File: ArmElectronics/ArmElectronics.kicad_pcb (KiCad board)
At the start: 2 copper layers, 101 x 139 mm, 97 parts, among them J1 Raspberry_Pi_2_3, J10 AH1815 Breakout, J11 AH1815 Breakout, J12 AH1815 Breakout, J13 AH1815 Breakout, J14 AH1815 Breakout, J15 AH1815 Breakout, J16 AH1815 Breakout, J17 AH1815 Breakout, J18 AH1815 Breakout, J19 AH1815 Breakout, J2 Conn_01x14, J20 AH1815 Breakout, J21 1792245, J22 PA-09, J23 PA-09, J24 PA-09, J25 Solenoid, J26 Stepper Alternate Connection, J27 Computer Fan, J28 Computer Fan, J3 Encoder Breakout, J4 RasPi Power Out, J5 12V In, J6 Batt In, J7 Batt Out, J8 BNO055 QWIIC Conn, J9 AH1815 Breakout, Q1 Q_NMOS_GDSD, SW1 E-Stop, U1 Teensy4.1, U12 74LVC1G97, U13 74LVC1G97, U14 74LVC1G97, U15 74LVC1G97, U16 74LVC1G97, U17 74LVC1G97, U2 Pololu_2857, U3 MAX11601, U4 Pololu_2851, U5 Pololu_3730, U6 TB9051FTG, U7 TB9051FTG, U8 TB9051FTG

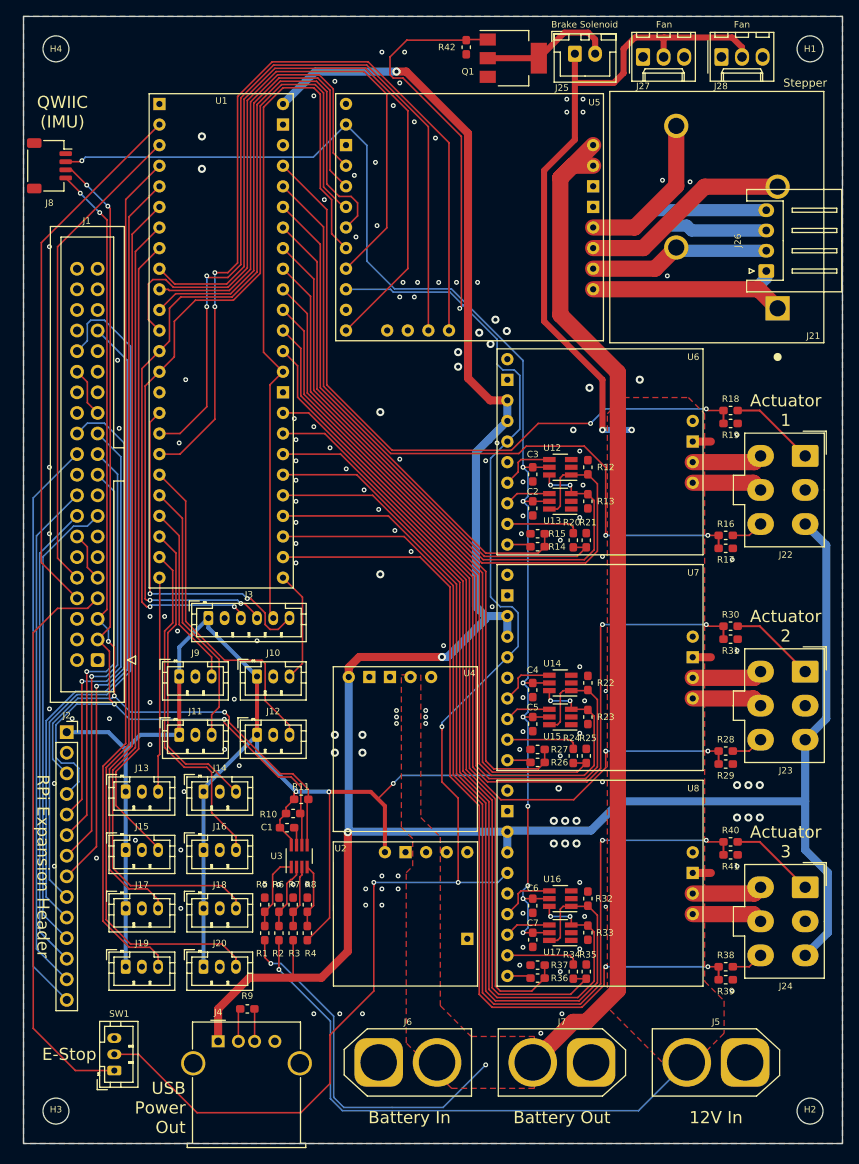
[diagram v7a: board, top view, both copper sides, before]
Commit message: Implemented post SAR fixes
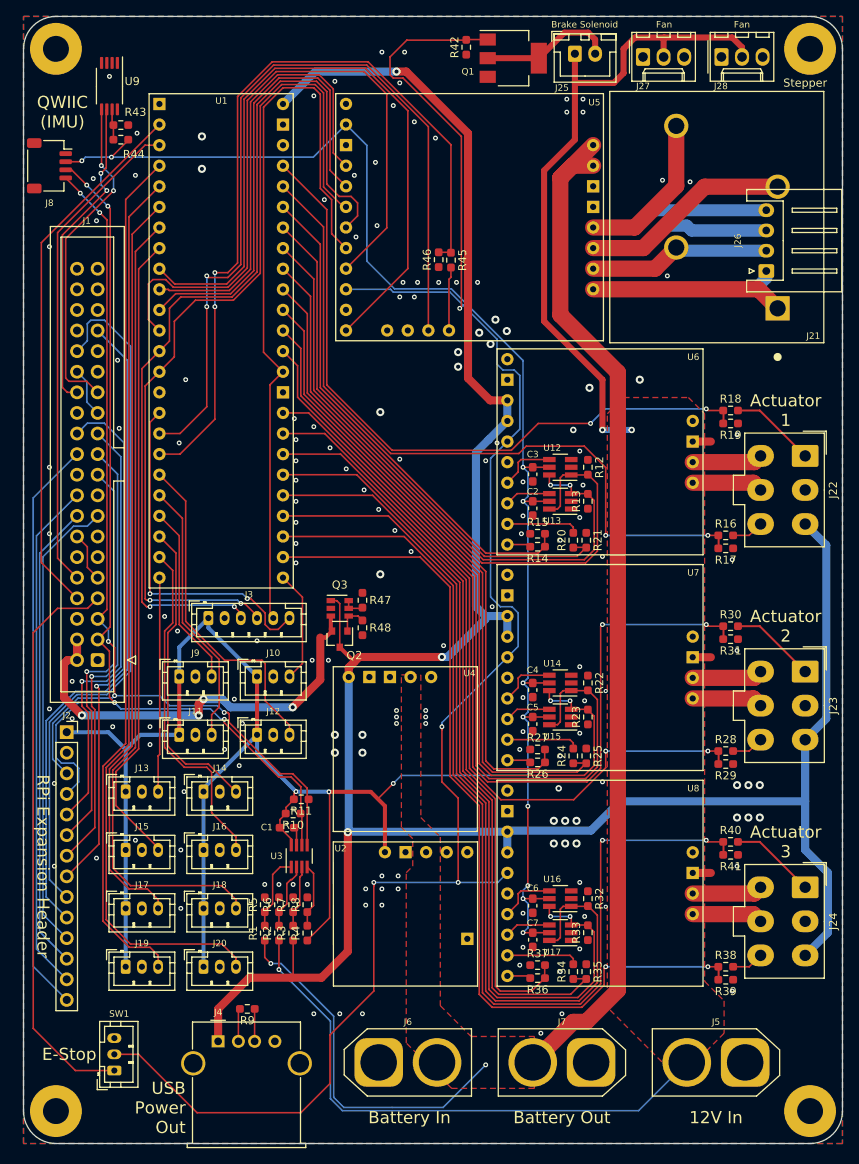
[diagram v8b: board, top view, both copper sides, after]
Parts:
- added Q2: Q_PMOS_GSD, Package_TO_SOT_SMD:SOT-23, F.Cu at (61.0, 105.8)
- added Q3: DMMT3906, Package_TO_SOT_SMD:SOT-23-6, F.Cu at (61.0, 102.0)
- added R43: DNP, Resistor_SMD:R_0603_1608Metric_Pad0.98x0.95mm_HandSolder, F.Cu at (34.0, 42.4)
- added R44: 10k, Resistor_SMD:R_0603_1608Metric_Pad0.98x0.95mm_HandSolder, F.Cu at (34.0, 44.2)
- added R45: 10k, Resistor_SMD:R_0603_1608Metric_Pad0.98x0.95mm_HandSolder, F.Cu at (74.7, 59.1)
- added R46: 10k, Resistor_SMD:R_0603_1608Metric_Pad0.98x0.95mm_HandSolder, F.Cu at (73.2, 59.0)
- added R47: 10k, Resistor_SMD:R_0603_1608Metric_Pad0.98x0.95mm_HandSolder, F.Cu at (63.8, 101.0)
- added R48: 47k, Resistor_SMD:R_0603_1608Metric_Pad0.98x0.95mm_HandSolder, F.Cu at (63.8, 104.4)
- added U9: CAT24C32, Package_SO:TSSOP-8_4.4x3mm_P0.65mm, F.Cu at (32.6, 37.6)
- H1, H2, H3, H4: footprint MountingHole:MountingHole_3.2mm_M3 -> MountingHole:MountingHole_3.2mm_M3_Pad
- J22, J23, J24: footprint ArmElectronics_Footprints:Molex_Mini-Fit_Jr_5566-06A_2x03_P4.20mm_Vertical_3D -> Connector_Molex:Molex_Mini-Fit_Jr_5566-06A_2x03_P4.20mm_Vertical
- R1: value 230k -> 240k; footprint Resistor_SMD:R_0603_1608Metric_Pad1.05x0.95mm_HandSolder -> Resistor_SMD:R_0603_1608Metric_Pad0.98x0.95mm_HandSolder
- R10, R11, R12, R13, R14, R15, R16, R17, R18, R19, R2, R20, R21, R22, R23, R24, R25, R26, R27, R28, R29, R3, R30, R31, R32, R33, R34, R35, R36, R37, R38, R39, R4, R40, R41, R42, R5, R6, R7, R8, R9: footprint Resistor_SMD:R_0603_1608Metric_Pad1.05x0.95mm_HandSolder -> Resistor_SMD:R_0603_1608Metric_Pad0.98x0.95mm_HandSolder
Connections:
- J1 pad 2: Net-(J1-Pad2) -> /5V_RPI
- J1 pad 27: Net-(J1-Pad27) -> /ID_SDA
- J1 pad 28: Net-(J1-Pad28) -> /ID_SCL
- J1 pad 4: Net-(J1-Pad4) -> /5V_RPI
- U5 pad 16: /Stepper_BEMF -> Net-(R45-Pad2)
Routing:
- net /5V_RPI: track 0.00 -> 53.4 mm, vias 0 -> 4
- net /ID_SDA: track 0.00 -> 40.9 mm, vias 0 -> 2
- net /ID_SCL: track 0.00 -> 39.2 mm, vias 0 -> 2
- net +5V: track 298.4 -> 307.5 mm
- net /Stepper_BEMF: track 105.7 -> 97.7 mm
- net Net-(R45-Pad2): track 0.00 -> 7.86 mm
- net Net-(Q2-Pad1): track 0.00 -> 3.83 mm
- net Net-(R43-Pad1): track 0.00 -> 3.80 mm
- net +3V3: track 351.9 -> 354.9 mm, vias 12 -> 13
- net Net-(Q3-Pad5): track 0.00 -> 2.69 mm
- net /RPi_RX: track 59.6 -> 60.6 mm
- net /RPi_SCLK0: track 52.7 -> 53.4 mm
- net GND: vias 155 -> 165
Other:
- outline, holes or cut-outs redrawn
- board text added: "Arm Base PCB r2 UAH SHC ASTRA"
- board text removed: "Arm Base PCB r1 UAH SHC ASTRA"
